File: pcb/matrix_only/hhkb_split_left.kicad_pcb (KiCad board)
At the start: 2 copper layers, 140.4 x 97.4 mm, 65 parts, among them SW1 CPG151101S11-2, SW10 CPG151101S11-2, SW11 CPG151101S11-2, SW12 CPG151101S11-2, SW13 CPG151101S11-2, SW14 CPG151101S11-2, SW15 CPG151101S11-2, SW16 CPG151101S11-2, SW17 CPG151101S11-2, SW18 CPG151101S11-2, SW19 CPG151101S11-2, SW2 CPG151101S11-2, SW20 CPG151101S11-2, SW21 CPG151101S11-2, SW22 CPG151101S11-2, SW23 CPG151101S11-2, SW24 CPG151101S11-2, SW25 CPG151101S11-2, SW26 CPG151101S11-2, SW27 CPG151101S11-2, SW3 CPG151101S11-2, SW4 CPG151101S11-2, SW5 CPG151101S11-2, SW6 CPG151101S11-2, SW7 CPG151101S11-2, SW8 CPG151101S11-2, SW9 CPG151101S11-2, U1 74LVC595

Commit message: 凍結を直し、列を戻すレーンを途中まで引いた
## 凍結の欠陥を 2 つ直した（どちらも私のもの）

1. **`protect` にしていた。**「動かすな」のつもりが **「触るな」** になり、
   Freerouting が**その線に繋ぎ込めなくなった。**COL→U1 が 6 本・
   ROW→J_DB が 5 本まるごと未配線として残った。
2. **`replay_matrix` が消しすぎていた。**ROW/COL の線を全部消してから
   写していたので、**Freerouting が引いた U1 へのスタブまで道連れ**に
   していた。消してよいのは「これから同じ場所へ置き直す線」だけ。

⚠️ **「Freerouting が引けていない」と報告したのは誤診だった。**
引けていたものを私が消していた。直した結果、右の未接続は 15 → 4。
凍結した 262 本は 1 本も欠けず、その上に Freerouting が 202 本
（1138mm）を足すようになった。**利用者の求めた切り分け（マトリクスは
手書き相当で凍結・それ以外は自動）が成立した。**

## 試しの配線を本番と別に出せるようにした

`autoroute.py --out pcb/try`。⚠️ **利用者「本番配線はまだ」と言われた
あとに本番 3 枚を上書きした**（git checkout で復元）。さらに
`--out pcb/matrix` で**利用者が手で置いた板まで上書きした**（KiCad の
履歴から復元）。**別フォルダに出すべきだった。**

## U1/U2 の位置（利用者の配置）を取り込んだ

  U1 (73.832, 96.455) / U2 (73.830,102.995) … J_DB の真下に縦一列
  C_U1/C_U2 はそれぞれの IC の真横（V3V3 まで 2.76 / 2.74mm）

**SPI が 89mm → 19mm に縮んだ**（利用者「SPI の波形は長く引きまわさない
方がいい／キーマトリクスはただの IO なので長くてもいい」——実測でも
その優先順位が正しい）。代償として列 8 本が基板を横断することになった。

## 列を戻すレーン（作業中・open-gaps #48）

**私の実装は失敗した**（DRC 42 件）。着地で U1 の他のパッドを横切り、
ビアが密集して互いに当たった。**利用者が手で 8 本引き直し**、私が
間隔を 0.95mm に均等化して右端を列へ繋いだ（ビア 8 個）。
成果物は `pcb/matrix_only/`。**左端の着地はこれから。**

死んだコードを消した: `FROZEN`（protect をやめて不要）と
`prewire_col_to_mcu`（失敗した実装・呼んでいない）。実測の記録は
open-gaps #48 へ移した。`test_constants` が緑に戻った。

pytest の赤 6 件は私の変更前と同じ（本番 pcb/ が未再生成＝#47）。

Co-Authored-By: Claude Opus 5 (1M context) <noreply@anthropic.com>
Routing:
- net GND: vias 4 -> 13

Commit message: 列のバスの形を揃えた（標準形を先に採る）
利用者「col のラインが、似ているが微妙に不規則です。なぜですか？」
→ **「余裕が最大の候補を選ぶ」という規則そのものが原因だった。**

`prewire_col_bus` は曲がる高さを 0.25〜0.5mm 刻みで振った候補を何十通りも
作り、そこから**穴との余裕が最大のもの**を選んでいた。周りの障害物
（隣のスイッチの胴・スタビ・取付穴）は**キーごとに少しずつ違う**ので、
**勝つ候補が列ごとに変わる。**実測で、同じ dx=+9.525 のホップが 3 本とも
違う形だった（曲がる y が 67.400 / 66.400 / 66.400、45° の使い方も別々）。

2026-08-17 に「穴とのギリギリ 0.330mm」を直したとき私が入れたもの。
隙間は揃ったが、**形の規則性を犠牲にしていた。**

## 直したこと

**形 A（縦 → 橋 → 縦 → 45° → 縦）の座標そのものを標準**と決め、通るなら
必ずそれを使う。通らないときだけ余裕の大きいものへ落とす（`_same_path`）。

    dx=+9.525  12 ホップ: 形 3 種類 → **10 本が完全に同一**
    dx=+4.763   5 ホップ: 形 3 種類 → **4 本が完全に同一**
    dx=+16.669  2 ホップ: 形 2 種類 → **2 本とも同一**
    区間数（左/右）: 103/122 → **82/99**
    配線由来の DRC: 0/2 → 0/2（変わらず）

## 残した例外（実測で確認・利用者「取り付け穴などの例外は除いて」）

    COL0 SW1→SW10   標準形だと H2（取付穴）に 0.269mm 食い込む
    COL0 SW10→SW18  同 J_DB に 0.777mm
    COL6 SW16→SW24  同 ST24（スタビ）に 1.586mm

COL0 が全体に短い（2〜3 区間）のは**行のバスを跨がない**ため（一番左の
列で、行がそこまで届いていない）。以前の指摘で直した意図的な差。

## pcb/matrix_only/ を更新した

マトリクスを新しい形に差し替えつつ、**利用者が引いたレーン 8 本は残した。**
⚠️ 最初の引き継ぎでレーンを 8 本とも消した——**レーンにも COL* の
ネットが付いている**ので「マトリクスの一部」と判定された。コミット済みの
版から復元し、「F.Cu の長い線は残す」を足して直した。
検証: マトリクスは unrouted と完全一致（左 192/192・右 239/239）。

Co-Authored-By: Claude Opus 5 (1M context) <noreply@anthropic.com>
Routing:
- net COL5: track 71.2 -> 67.0 mm
- net COL2: track 70.7 -> 67.0 mm
- net COL3: track 94.4 -> 93.8 mm
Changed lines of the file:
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@@
 	)
 	(segment
-		(start 159.58375 66.2)
-		(end 159.58375 66.4)
-		(width 0.2)
-		(layer "B.Cu")
-		(net "COL4")
-	)
-	(segment
-		(start 173.87125 104.3)
-		(end 173.87125 104.5)
-		(width 0.2)
-		(layer "B.Cu")
-		(net "COL4")
-	)
-	(segment
-		(start 168.83375 75.65)
-		(end 169.10875 75.65)
-		(width 0.2)
-		(layer "B.Cu")
-		(net "COL4")
-	)
-	(segment
-		(start 183.12125 113.75)
-		(end 183.39625 113.75)
+		(start 169.10875 85.25)
+		(end 169.10875 92.697499)
 		(width 0.2)
 		(layer "B.Cu")
@@
 	)
 	(segment
-		(start 169.10875 88.1)
-		(end 173.87125 92.8625)
+		(start 159.58375 68.884999)
+		(end 169.10875 78.409999)
 		(width 0.2)
 		(layer "B.Cu")
@@
 	)
 	(segment
-		(start 173.87125 104.5)
-		(end 183.12125 113.75)
-		(width 0.2)
-		(layer "B.Cu")
-		(net "COL4")
-	)
-	(segment
-		(start 159.58375 66.4)
-		(end 168.83375 75.65)
-		(width 0.2)
-		(layer "B.Cu")
-		(net "COL4")
-	)
-	(segment
-		(start 173.87125 92.8625)
+		(start 173.87125 106.984998)
+		(end 183.39625 116.509999)
+		(width 0.2)
+		(layer "B.Cu")
+		(net "COL4")
+	)
+	(segment
+		(start 169.10875 92.697499)
 		(end 173.87125 97.46)
 		(width 0.2)
@@
 	)
 	(segment
-		(start 169.10875 75.65)
-		(end 169.10875 78.409999)
-		(width 0.2)
-		(layer "B.Cu")
-		(net "COL4")
-	)
-	(segment
-		(start 183.39625 113.75)
-		(end 183.39625 116.509999)
-		(width 0.2)
-		(layer "B.Cu")
-		(net "COL4")
-	)
-	(segment
-		(start 169.10875 85.25)
-		(end 169.10875 88.1)
+		(start 173.87125 104.3)
+		(end 173.87125 106.984998)
+		(width 0.2)
+		(layer "B.Cu")
+		(net "COL4")
+	)
+	(segment
+		(start 159.58375 66.2)
+		(end 159.58375 68.884999)
 		(width 0.2)
 		(layer "B.Cu")
@@
 	)
 	(segment
-		(start 140.533749 66.4)
-		(end 149.783749 75.65)
-		(width 0.2)
-		(layer "B.Cu")
-		(net "COL3")
-	)
-	(segment
-		(start 154.30875 96.2)
-		(end 154.82125 96.2)
-		(width 0.2)
-		(layer "B.Cu")
-		(net "COL3")
-	)
-	(segment
-		(start 154.82125 104.5)
-		(end 164.07125 113.75)
-		(width 0.2)
-		(layer "B.Cu")
-		(net "COL3")
-	)
-	(segment
-		(start 164.346249 113.75)
-		(end 164.346249 116.509999)
+		(start 140.533749 66.2)
+		(end 140.533749 68.884998)
 		(width 0.2)
 		(layer "B.Cu")
@@
 	(segment
 		(start 154.82125 104.3)
-		(end 154.82125 104.5)
-		(width 0.2)
-		(layer "B.Cu")
-		(net "COL3")
-	)
-	(segment
-		(start 164.07125 113.75)
-		(end 164.346249 113.75)
+		(end 154.82125 106.984999)
 		(width 0.2)
 		(layer "B.Cu")
@@
 	)
 	(segment
+		(start 154.82125 106.984999)
+		(end 164.346249 116.509999)
+		(width 0.2)
+		(layer "B.Cu")
+		(net "COL3")
+	)
+	(segment
 		(start 164.346249 116.509999)
 		(end 164.346249 122.05)
@@
 	)
 	(segment
-		(start 149.783749 75.65)
-		(end 150.05875 75.65)
-		(width 0.2)
-		(layer "B.Cu")
-		(net "COL3")
-	)
-	(segment
-		(start 140.533749 66.2)
-		(end 140.533749 66.4)
-		(width 0.2)
-		(layer "B.Cu")
-		(net "COL3")
-	)
-	(segment
-		(start 150.05875 91.95)
-		(end 154.30875 96.2)
+		(start 150.05875 85.25)
+		(end 150.05875 92.6975)
+		(width 0.2)
+		(layer "B.Cu")
+		(net "COL3")
+	)
+	(segment
+		(start 140.533749 68.884998)
+		(end 150.05875 78.409999)
 		(width 0.2)
 		(layer "B.Cu")
@@
 	)
 	(segment
-		(start 150.05875 75.65)
-		(end 150.05875 78.409999)
-		(width 0.2)
-		(layer "B.Cu")
-		(net "COL3")
-	)
-	(segment
-		(start 150.05875 85.25)
-		(end 150.05875 91.95)
-		(width 0.2)
-		(layer "B.Cu")
-		(net "COL3")
-	)
-	(segment
-		(start 154.82125 96.2)
+		(start 150.05875 92.6975)
 		(end 154.82125 97.46)
 		(width 0.2)
@@
 	)
 	(segment
-		(start 131.008749 85.25)
-		(end 131.008749 86.999999)
-		(width 0.2)
-		(layer "B.Cu")
-		(net "COL2")
-	)
-	(segment
 		(start 135.77125 97.46)
 		(end 135.77125 103)
@@
 	)
 	(segment
-		(start 124.73375 69.65)
-		(end 131.008749 69.65)
-		(width 0.2)
-		(layer "B.Cu")
-		(net "COL2")
-	)
-	(segment
-		(start 131.008749 69.65)
-		(end 131.008749 78.409999)
+		(start 121.48375 66.2)
+		(end 121.48375 68.884999)
 		(width 0.2)
 		(layer "B.Cu")
@@
 	)
 	(segment
-		(start 135.77125 104.3)
-		(end 135.77125 106.05)
-		(width 0.2)
-		(layer "B.Cu")
-		(net "COL2")
-	)
-	(segment
-		(start 131.008749 86.999999)
-		(end 135.77125 91.7625)
-		(width 0.2)
-		(layer "B.Cu")
-		(net "COL2")
-	)
-	(segment
 		(start 121.48375 59.359999)
 		(end 121.48375 64.899999)
@@
 	)
 	(segment
-		(start 145.29625 115.574999)
+		(start 135.77125 104.3)
+		(end 135.77125 106.984999)
+		(width 0.2)
+		(layer "B.Cu")
+		(net "COL2")
+	)
+	(segment
+		(start 131.008749 85.25)
+		(end 131.008749 92.697499)
+		(width 0.2)
+		(layer "B.Cu")
+		(net "COL2")
+	)
+	(segment
+		(start 121.48375 68.884999)
+		(end 131.008749 78.409999)
+		(width 0.2)
+		(layer "B.Cu")
+		(net "COL2")
+	)
+	(segment
+		(start 131.008749 92.697499)
+		(end 135.77125 97.46)
+		(width 0.2)
+		(layer "B.Cu")
+		(net "COL2")
+	)
+	(segment
+		(start 135.77125 106.984999)
 		(end 145.29625 116.509999)
-		(width 0.2)
-		(layer "B.Cu")
-		(net "COL2")
-	)
-	(segment
-		(start 135.77125 106.05)
-		(end 145.29625 115.574999)
-		(width 0.2)
-		(layer "B.Cu")
-		(net "COL2")
-	)
-	(segment
-		(start 135.77125 91.7625)
-		(end 135.77125 97.46)
-		(width 0.2)
-		(layer "B.Cu")
-		(net "COL2")
-	)
-	(segment
-		(start 121.48375 66.2)
-		(end 121.48375 66.4)
-		(width 0.2)
-		(layer "B.Cu")
-		(net "COL2")
-	)
-	(segment
-		(start 121.48375 66.4)
-		(end 124.73375 69.65)
 		(width 0.2)
 		(layer "B.Cu")
@@
 	)
 	(segment
-		(start 192.40875 94.2)
-		(end 192.92125 94.2)
-		(width 0.2)
-		(layer "B.Cu")
-		(net "COL5")
-	)
-	(segment
-		(start 188.15875 69.65)
+		(start 192.92125 104.3)
+		(end 192.92125 106.984998)
+		(width 0.2)
+		(layer "B.Cu")
+		(net "COL5")
+	)
+	(segment
+		(start 178.63375 68.884999)
 		(end 188.15875 78.409999)
-		(width 0.2)
-		(layer "B.Cu")
-		(net "COL5")
-	)
-	(segment
-		(start 188.15875 85.25)
-		(end 188.15875 89.95)
 		(width 0.2)
 		(layer "B.Cu")
@@
 	)
 	(segment
-		(start 192.92125 104.3)
-		(end 192.92125 104.5)
-		(width 0.2)
-		(layer "B.Cu")
-		(net "COL5")
-	)
-	(segment
-		(start 192.92125 94.2)
+		(start 188.15875 85.25)
+		(end 188.15875 92.6975)
+		(width 0.2)
+		(layer "B.Cu")
+		(net "COL5")
+	)
+	(segment
+		(start 192.92125 106.984998)
+		(end 202.44625 116.509999)
+		(width 0.2)
+		(layer "B.Cu")
+		(net "COL5")
+	)
+	(segment
+		(start 188.15875 92.6975)
 		(end 192.92125 97.46)
-		(width 0.2)
-		(layer "B.Cu")
-		(net "COL5")
-	)
-	(segment
-		(start 181.88375 69.65)
-		(end 188.15875 69.65)
-		(width 0.2)
-		(layer "B.Cu")
-		(net "COL5")
-	)
-	(segment
-		(start 178.63375 66.2)
-		(end 178.63375 66.4)
-		(width 0.2)
-		(layer "B.Cu")
-		(net "COL5")
-	)
-	(segment
-		(start 202.17125 113.75)
-		(end 202.44625 113.75)
-		(width 0.2)
-		(layer "B.Cu")
-		(net "COL5")
-	)
-	(segment
-		(start 192.92125 104.5)
-		(end 202.17125 113.75)
 		(width 0.2)
 		(layer "B.Cu")
@@
 	)
 	(segment
-		(start 178.63375 66.4)
-		(end 181.88375 69.65)
-		(width 0.2)
-		(layer "B.Cu")
-		(net "COL5")
-	)
-	(segment
-		(start 188.15875 89.95)
-		(end 192.40875 94.2)
-		(width 0.2)
-		(layer "B.Cu")
-		(net "COL5")
-	)
-	(segment
-		(start 202.44625 113.75)
-		(end 202.44625 116.509999)
-		(width 0.2)
-		(layer "B.Cu")
+		(start 178.63375 66.2)
+		(end 178.63375 68.884999)
+		(width 0.2)
+		(layer "B.Cu")

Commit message: どこにも繋がっていない GND ビアを既定で打たなくした
利用者「どこにもつながってない GND ビアを一旦入れないようにしてほしいです。
それは最後にやる工程なはずなので。」

`gnd_fanout.stitch_islands` が打つ離島の縫い止めは、**ベタ以外の何にも
触れていない。**配線が動けばベタの形が変わり、要らなくなる／別の場所に
要る。**しかも浮いたビアはこれから引く配線の邪魔をする。**

→ **既定では打たない。**配線が固まってから最後に 1 回だけ:

    GND_STITCH=1 "$KPY" tools/gen_pcb.py

紛れ込んだ浮きビアを落とす `_drop_stitch_vias()` も足した。判定は
「GND のパッドにも GND の配線にも触れていないビア」。**`gnd_fanout.place`
のファンアウト（GND パッドの真横）は残る**——あれはパッドに繋がっている。

## 効いていることを数えた

ビアの総数（`(via` の行数）:

    左   既定 38  /  GND_STITCH=1  74   差 36
    右   既定 95  /  GND_STITCH=1 155   差 60

**この差が、これまで入っていた浮きビア。**「打たない設定にした」だけでは
効いた証拠にならないので、両方を出して数えた。

## 副作用が無いことを確かめた

利用者が引いた配線（pcb/matrix_routing.json）と照合:

    left:  配線 158 中 失った 0 / ビア 34 中 失った 0
    right: 配線 353 中 失った 0 / ビア 89 中 失った 0

⚠️ **これから DRC に `isolated_copper` が出る**（左 36 / 右 60 相当）。
縫っていないので出るのが正しい。**これを見て「壊れた」と思わないこと。**

⚠️ 本番の pcb/ は触っていない（pcb/unrouted/ と pcb/matrix_only/ のみ）。

Co-Authored-By: Claude Opus 5 (1M context) <noreply@anthropic.com>
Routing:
- net GND: vias 13 -> 4

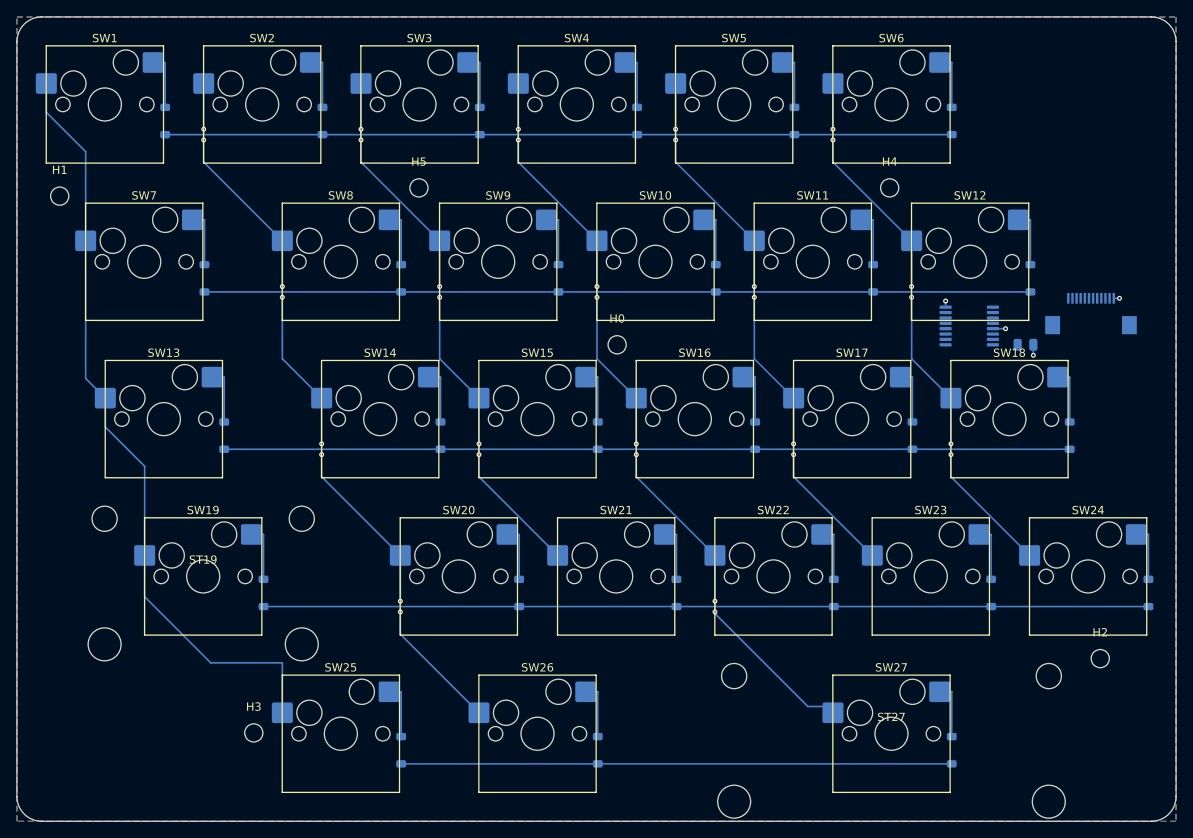
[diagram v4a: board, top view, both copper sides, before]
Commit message: 配線を塞いでいた取付穴 2 つを動かした（右 H0 / H2）
利用者「col 接続用の横ラインの途中に、基板の穴があります。非常に邪魔」
「1 行 1 列のところにある穴も、少し調節して、ROW0 への配線が綺麗になるように」

## なぜ塞いでいたか

**穴を決めたときの目的関数に「配線」が入っていなかった**（2026-08-12）。
当時は「キーから最寄りの留め点までの最大距離を小さくする」の 1 本だけで、
**横ライン（COL → U1/U2）はまだ存在しなかった。**あとから引いた線が
穴にぶつかった。**5 つ目の条件が増えた。**

    H0  (0.00, 10.00) → (0.00, 28.00)    配線まで 0.675 → 1.607mm
    H2  (-77.00, 26.50) → (-82.40, 26.50) 配線まで 0.460 → 2.540mm

**H0 は横ラインの帯（板 y=86.2..92.9）の真ん中に立っていた。**

**H2 は ROW0 の縦降りを挟んでいた。**⚠️ **ROW0 は `ROW_A` ではなく
`ROW_C`**（D1 の接続先で確かめた。名前と行番号は一致しない）。

## H0 は「規則」で選んだ。数字が最良だからではない

利用者に「H0 以外に、H0 と規則的に並んでいる穴があるんですか？」と
問われて調べたら、**H0 は他のどの穴とも x も y も揃っていなかった。**
「並びが崩れる」という私の反対理由は**誤りだった。**

**揃っているのは y=28 の 3 個**（H7 -38 / H6 38 / H3 81）で、
**x は -38 / 38 が 38mm 等間隔。その真ん中の x=0 が空席だった。**
銅までの隙間は (9.10, 29.00) の 2.36mm が最良だが、**規則に載る
(0.00, 28.00) を採った**（1.61mm でも帯から 14mm 外れる）。

## H2 は「縁」と「配線」の折り合い

⚠️ **この 2 つは真正面から競合する**（ROW_C の F.Cu 縦降りが板 x=71.34）。
一度 x=-84.65 まで逃がして配線 4.79mm を得たが、利用者「基板端すぎる」。
**縁 3.40mm を取って配線 2.54mm。**x=-79.90 まで戻すと配線 0.04mm で落ちる。

**どちらもキーからの最大距離 35.33mm を悪化させていない**（動かす前と同じ）。

## この移動で 1 件出た課題: 名札がキーの枠に重なっていた

H0 を動かしたら `silk_overlap` が 1 件増えた。**取付穴の名札は既定で
穴の 3.15mm 手前に出るが、そこはすぐ手前のキーの枠の中**だった。
**同じものが前から 4 件出ていた**（H1/H3/H6/H7）。警告なので誰も見ていない。
**5 件目を作って初めて 4 件に気づいた。**

→ `_place_hole_label` が手前・奥・左・右を試し、**当たらない向きへ回す。**
全部当たるなら既定のまま（**名札を消して黙らせない**。消すと穴が識別できない）。

    silk_overlap  右 13 → 9 ／ 左 7 → 3（取付穴がらみは 0）

⚠️ **故意に壊して確かめた。**逃がし先を 1 方向だけにすると DRC が 5 件出す。

## 測ったこと

    DRC 前後差       増えた違反 0 件 ／ 消えた 4 件
    利用者の配線     左 158+34 ・右 353+89  失った 0
    柱 φ4 と全 73 部品のコートヤード  8 本とも当たらない（最小 2.655mm）
    プレートの STL   新 8 か所に柱 ／ **旧 2 か所は頂点 0**（残っていない）
    組み立て STL     平らな板と x の値の集合が完全一致・柱の頂点数も全一致

CAD の生成物も出し直した（STL・build/plate_*.stl・.blend）。
⚠️ **refresh_view.sh は build/plate_*.stl を出さない。**放っておくと
8/17 のまま残る（実際に古い位置の柱が入っていた）。gen_plate.py を別に叩く。

## 検査

**16 件赤。うち 15 件は自分より前から赤**（git stash して確認）。
残る 1 件 `test_the_pcb_is_actually_fastened_to_the_plate[right]` は
「H0 に ic_tssop16 が当た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
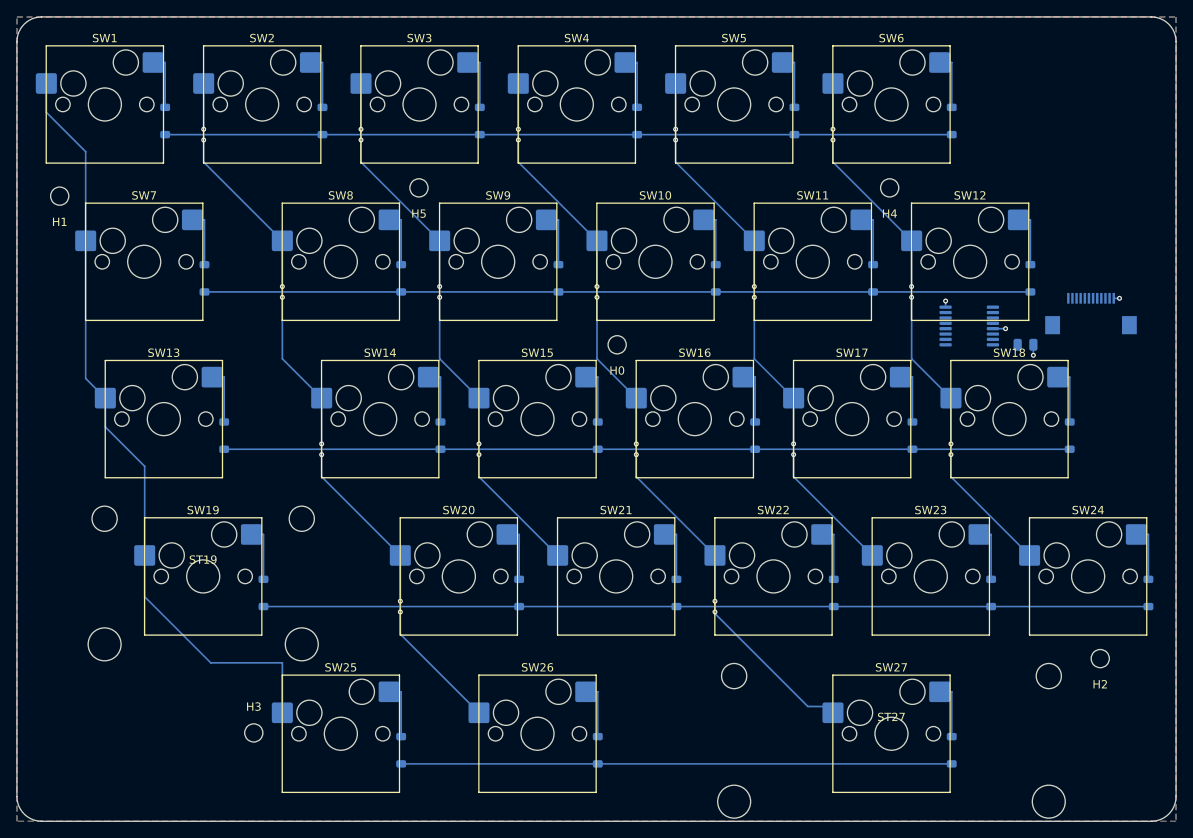
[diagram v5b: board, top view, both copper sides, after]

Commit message: 両手とも決定的な配置配線が揃った（左右ともエラー 0・未配線 0）
利用者「これで一旦、決定的な配置配線は、右手に限り完了した」
「このノウハウを、左手に展開してください」→ 展開 → 利用者が左右とも仕上げ。

    左  エラー 0 / 未配線 0   配線 279 区間・ビア 62・GND 4+スタブ 5
    右  エラー 0 / 未配線 0   配線 349 区間・ビア 87・GND 7+スタブ 8

## 左へ展開したこと

**取付穴 H0 を帯の外へ。**(2.50, 9.00) → **(2.50, -9.00)**。
⚠️ **右と同じ答えにはならなかった。**右は「y=28 の既存の列に載せる」が
正解だったが、**左は穴が 6 本しか無く H0 が中央の支えを兼ねている。**
y=28 へ動かすと**キーからの最大距離が 34.36 → 47.05mm** に悪化する。
**x はそのまま y を符号反転**（帯の反対側）で **34.36 → 31.01mm**。
**手順は同じでも答えは測って出す。**

**横ライン 6 本。**間隔 0.95mm 均一・右端 189.000 統一・完全な降順。
⚠️ **右は昇順、左は降順。**U1 のパッドが左は上から COL5→COL1 だから
（鏡像なので逆になる）。扇形の開きは最大 0.600mm（右は 1.700mm）。

## 利用者が仕上げたこと

**左**: 扇形 6 本・ROW 5 本・V3V3/SPI/CS/SPARE を全部接続（+93 区間）。
C_U1 を U1 の上へ寄せた（板 201.950,91.000 → 201.070,86.500）。
**J_DB 手前の詰まりを、ビアを階段状に散らして解いた**——
私が「どの径でも成立しない」と言った ROW_D が **0.150 → 0.319mm**。
**径ではなく位置で解くのが正解だった。**ビアも全部 φ0.6 に統一。

**右**: **レーン左端の余分なビア 7 個を削除。**私が置いたもので、
**両側が F.Cu ＝ 層をまたがないので意味が無い**（`via_dangling` 7→2）。
SPARE/SPARE2 を J_DB へ接続。

## スクリプト側

`export_matrix_routing.py`
  * **GND のビアとスタブも写す。**利用者が V3V3 から離した位置
    （0.302/0.312mm → 1.26〜1.86mm）が、次の生成で消えていた。
    ⚠️ **「電源から N mm 離す」という規則にして失敗した**——候補を弾くと
    逆に V3V3 の**配線**側へ押し出され、7 個中 4 個が落ちて U1/U2 の
    GND パッドがベタに繋がらなくなった。`gnd_fanout.py` は元へ戻した。
    **パッドしか見ない探索に、配線の都合は表現できない。現物を写す。**
  * **アニュラー不足のビアを規格まで広げる。**KiCad の既定ビアは
    φ0.5/穴 0.3 でアニュラー 0.100mm、JLC の下限は 0.130mm。
    **手で引くと必ず踏む**（実測 左 10・右 1）。穴は変えない。
    ⚠️ **標準の φ0.6 へ揃えたら `clearance` が 2 件出た。**詰まった場所は
    太らせる余地が無い。**規格を満たす最小に留める。**

`gen_pcb.py`
  * `apply_matrix_routing` が GND のビアとスタブも載せる。
  * `_drop_gnd_vias_hitting` が**スタブの線も落とす**。ビアだけ消すと
    線が残り、あとから載る配線と `tracks_crossing` になった。

`pcb_rules.py`  DECOUPLE_OFFSET["left"]["C_U1"] を利用者の位置へ。

## 一致を数えた

    left  GND 以外 341/341  GND  9/9    差 0（SPARE 2 本が 0.001mm の丸め）
    right GND 以外 436/436  GND 15/15   差 0

## 直した取りこぼし

**COL の斜め線が編集中に消えていた**（縦バス下端 → 下の行）。
右 4 本・左 5 本。元の座標のまま戻した。`ROW_A` の孤児 1 本は削除。

⚠️ `isolated_copper`（左 47・右 62）は**縫いビアを既定で打たない設定**
（利用者「それは最後にやる工程」）。`GND_STIT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
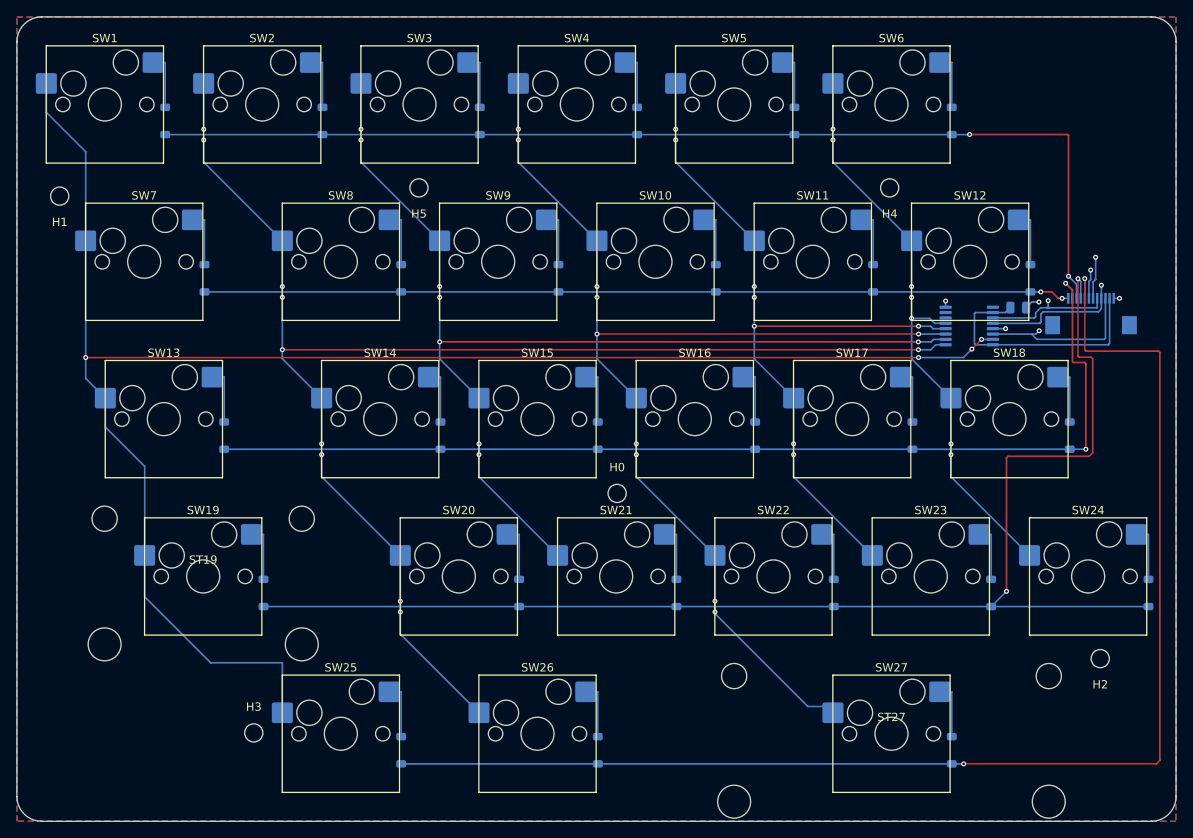
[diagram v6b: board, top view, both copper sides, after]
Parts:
- moved H0 18.0 mm to (152.5, 109.0)
- moved C_U1 4.59 mm to (201.1, 86.5)
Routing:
- net COL0: track 93.1 -> 203.9 mm, vias 0 -> 4
- net ROW_A: track 66.7 -> 161.7 mm, vias 0 -> 2
- net COL1: track 90.0 -> 170.6 mm, vias 8 -> 10
- net COL2: track 67.0 -> 128.4 mm, vias 6 -> 8
- net ROW_B: track 107.2 -> 161.9 mm, vias 0 -> 2
- net COL3: track 93.8 -> 136.0 mm, vias 8 -> 10
- net ROW_C: track 95.3 -> 129.7 mm, vias 0 -> 2
- net V3V3: track 0.00 -> 30.2 mm
- net ROW_D: track 102.4 -> 128.4 mm, vias 0 -> 2
- net COL4: track 67.0 -> 90.3 mm, vias 6 -> 8
- net SPI_MOSI: track 0.00 -> 19.9 mm, vias 0 -> 1
- net CS: track 0.00 -> 17.3 mm, vias 0 -> 1
- net SPI_SCK: track 0.00 -> 15.7 mm, vias 0 -> 1
- net SPARE2: track 0.00 -> 5.10 mm, vias 0 -> 1
- net ROW_E: track 100.0 -> 104.9 mm, vias 0 -> 2
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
